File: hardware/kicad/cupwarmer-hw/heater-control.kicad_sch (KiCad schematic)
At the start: 8 parts, among them Q1 AO3400 SOT-23

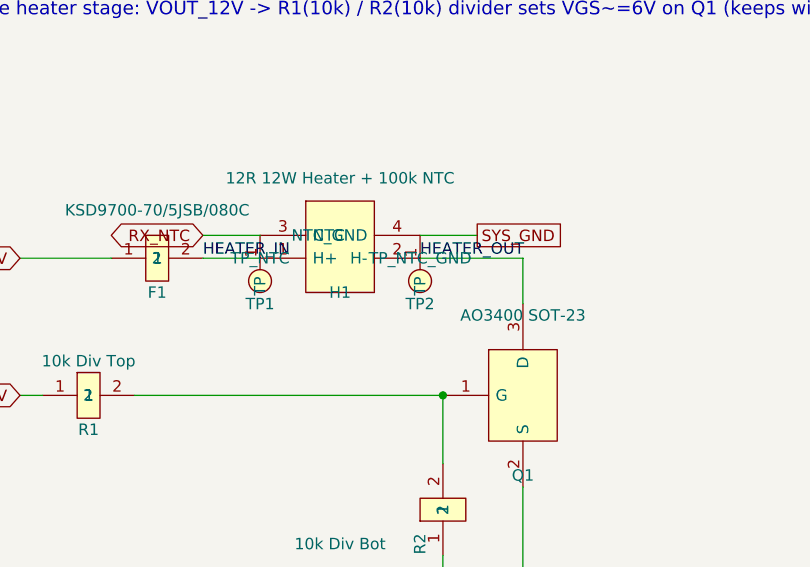
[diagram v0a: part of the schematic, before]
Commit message: Move F1 thermostat and TH2 NTC off-board
F1 (KSD9700 thermostat) and TH2 (heater NTC) are now part of the
heater assembly rather than the cupwarmer PCB; they ship together
with the JLCPCB silicone heater order. Drop F1's PCB footprint,
flip the schematic symbol to on_board=no, and add TH2 to the BOM
as an off-board NTC. Document R7=51k sizing for the OTP divider.

Co-Authored-By: Claude Opus 4.7 (1M context) <noreply@anthropic.com>
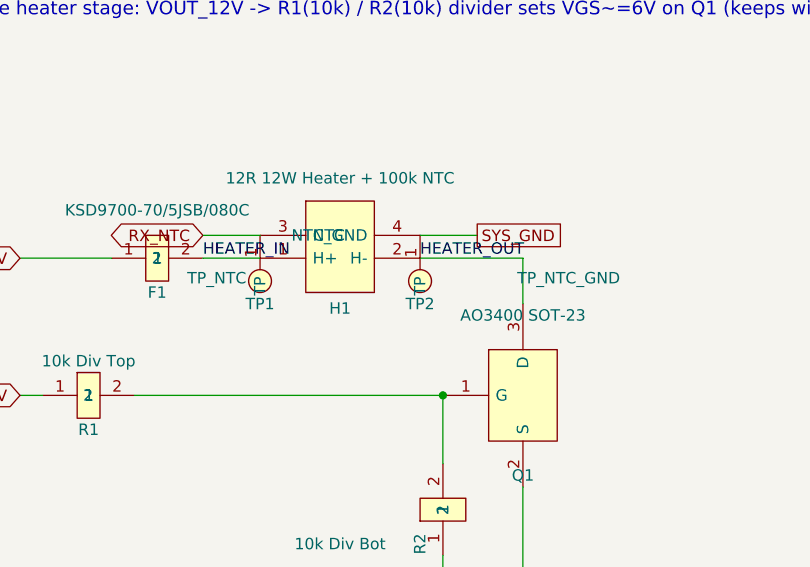
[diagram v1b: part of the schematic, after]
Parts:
- F1: footprint Connector_Wire:SolderWire-0.5sqmm_1x02_P4.8mm_D0.9mm_OD2.3mm -> (none)
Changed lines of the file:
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@@
 		(exclude_from_sim no)
 		(in_bom yes)
-		(on_board yes)
+		(on_board no)
 		(in_pos_files yes)
 		(dnp no)
@@
 			)
 		)
-		(property "Footprint" "Connector_Wire:SolderWire-0.5sqmm_1x02_P4.8mm_D0.9mm_OD2.3mm"
+		(property "Footprint" ""
 			(at 55.88 58.42 0)
 			(hide yes)
@@
 		(dnp no)
 		(property "Reference" "H1"
-			(at 76.2 62.23 0)
+			(at 76.2 64 0)
 			(show_name no)
 			(do_not_autoplace no)
@@
 		)
 		(property "Value" "TP_NTC"
-			(at 67.31 58.42 0)
+			(at 62.5 60.63 0)
 			(show_name no)
 			(do_not_autoplace no)
@@
 		)
 		(property "Value" "TP_NTC_GND"
-			(at 85.09 58.42 0)
-			(show_name no)
-			(do_not_autoplace no)
+			(at 101.6 60.63 0)
+			(show_name no)
+			(do_not_autoplace no)
